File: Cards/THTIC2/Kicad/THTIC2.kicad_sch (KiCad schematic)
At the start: 26 parts, among them J1 Conn_01x04_Pin, J2 Plasma 300V, U1 B0509S-1WR3, U2 ISO1540, U3 ADS1014IDGS, U4 AMS1117-5, U5 LMV321

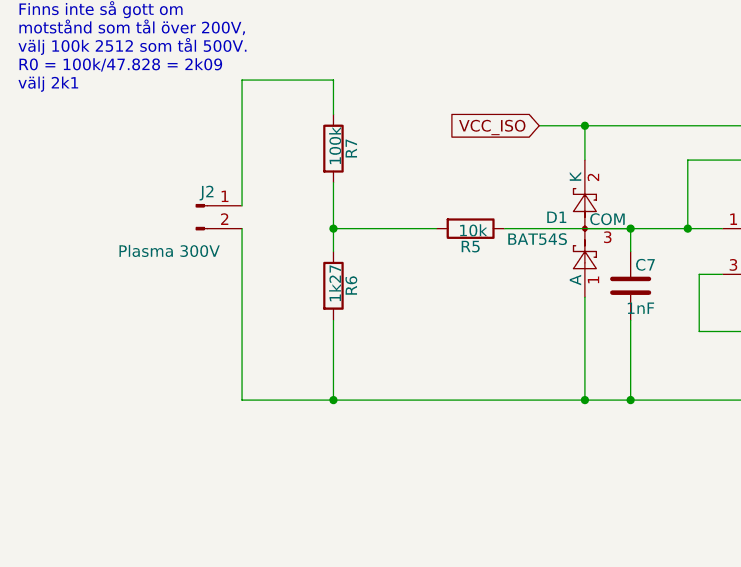
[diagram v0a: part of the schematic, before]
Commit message: Name change of E7000
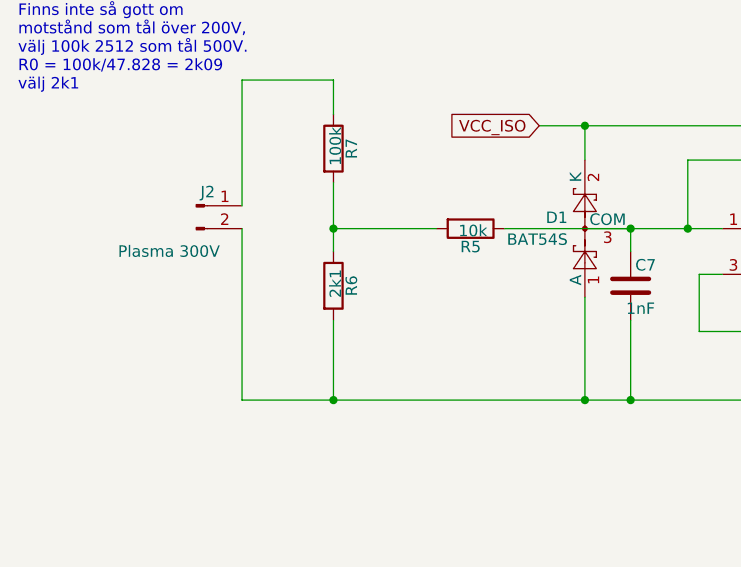
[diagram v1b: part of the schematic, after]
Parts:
- R6: value 1k27 -> 2k1
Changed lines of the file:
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@@
 			)
 		)
-		(property "Value" "1k27"
+		(property "Value" "2k1"
 			(at 52.324 82.296 90)
 			(effects

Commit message: Final version of THTIC2
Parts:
- added R8: 2k2, Resistor_SMD:R_0805_2012Metric, symbol Device:R
- R4: value nP -> 2k2
- renumbered H2 to H4
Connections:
- net 5V: now also R4.1, R8.1
- net at C7.1, D1.3 (COM), R5.1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: no longer R4.2
- net at R3.2, U5.3 (-), U5.4: no longer R4.1
- net at J1.2 (Pin_2), U2.2 (SDA1): now also R4.2
- net at J1.3 (Pin_3), U2.3 (SCL1): now also R8.2
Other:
- note added: "Optional pullups"
- moved on the sheet: J1

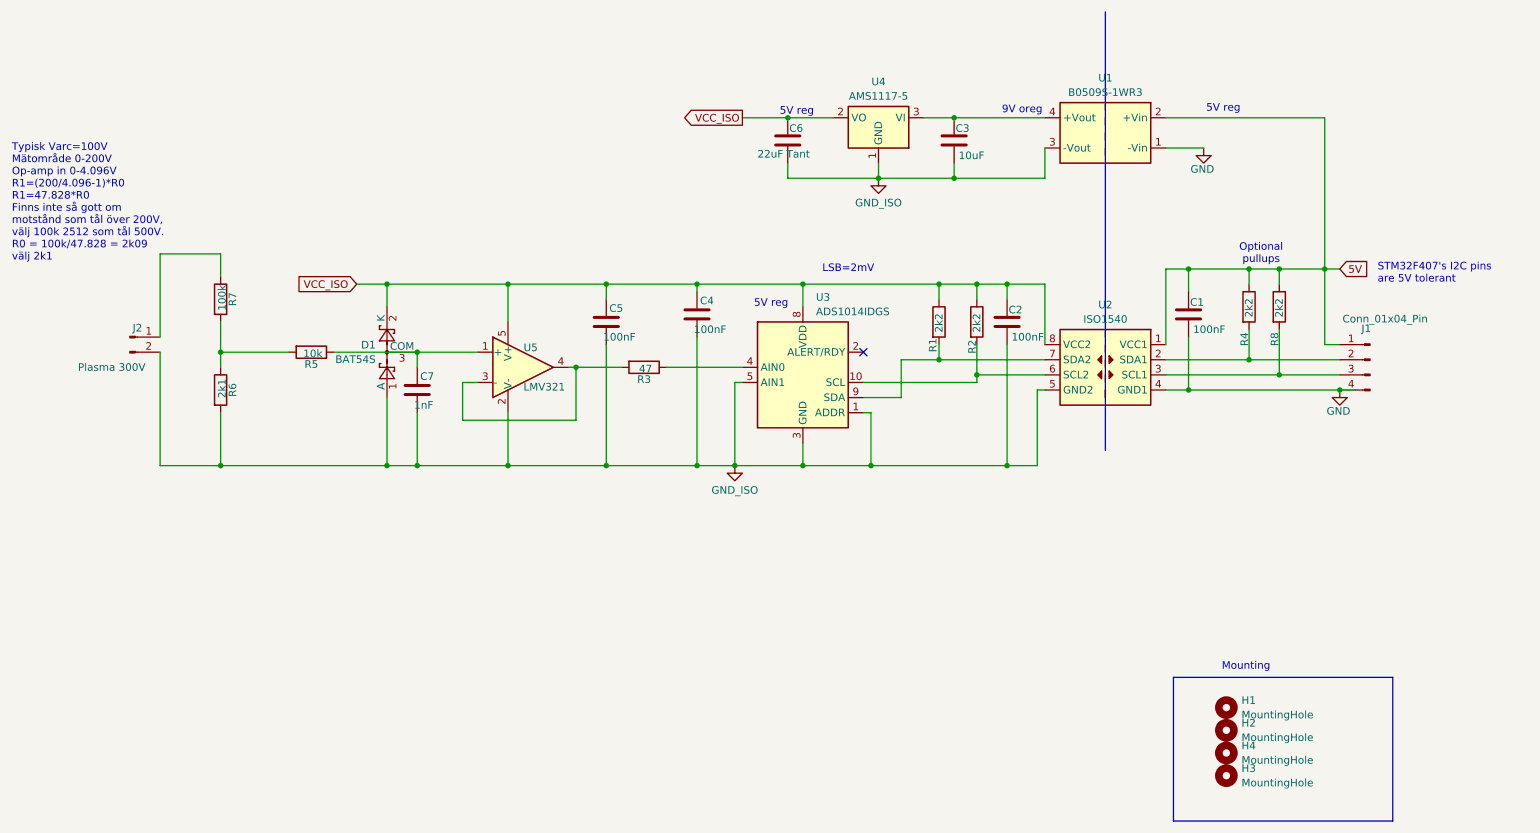
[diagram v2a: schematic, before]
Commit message: Now measuring 0 - -200 Volts.
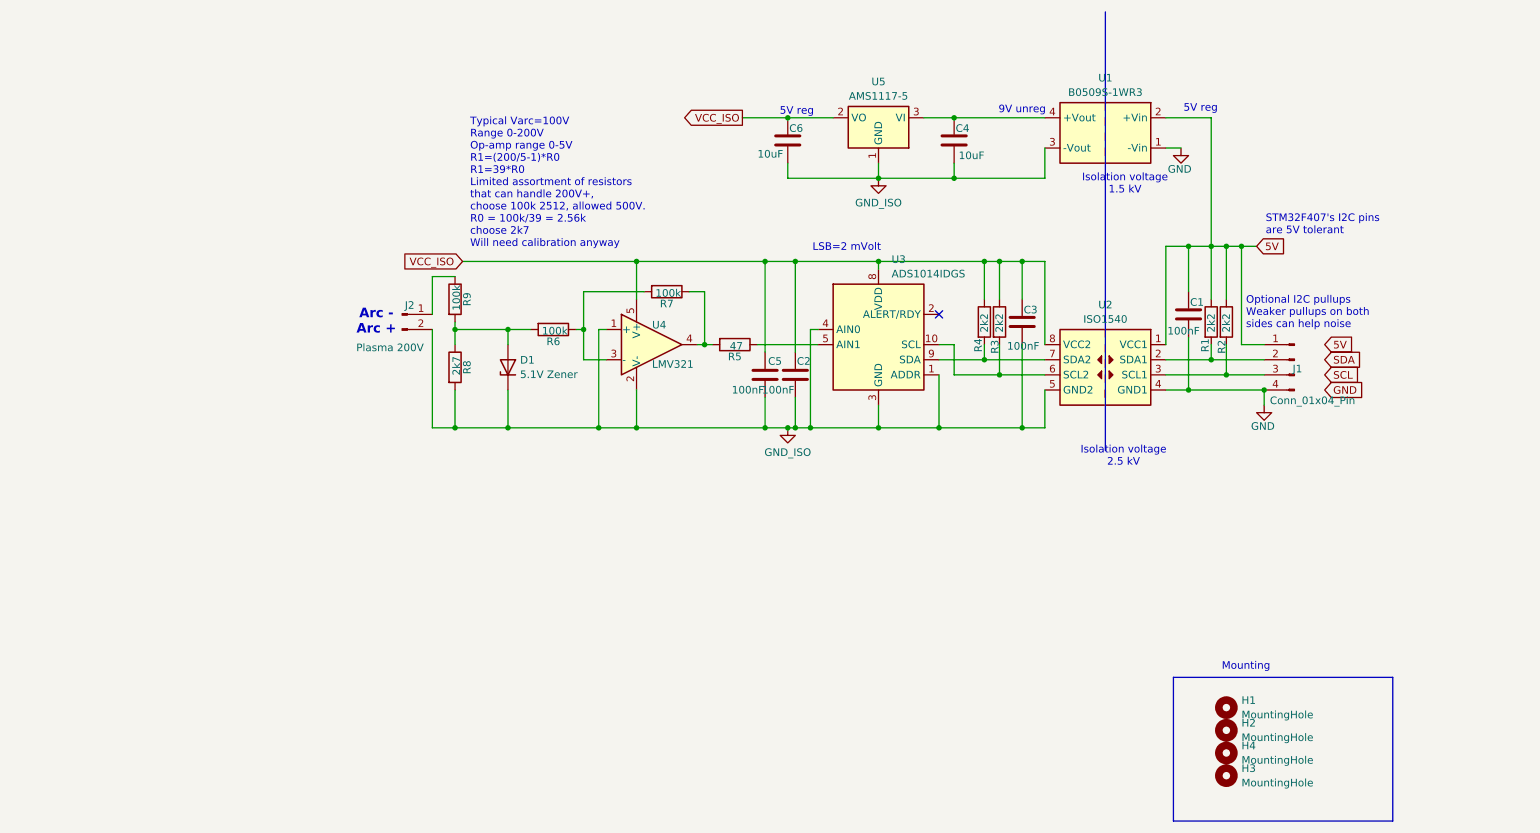
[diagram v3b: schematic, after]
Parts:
- removed C5: 100nF, Capacitor_SMD:C_0805_2012Metric, symbol Device:C
- removed C7: 1nF, Capacitor_SMD:C_0805_2012Metric, symbol Device:C
- removed D1: BAT54S, Package_TO_SOT_SMD:SOT-23, symbol Diode:BAT54S
- removed R4, R8: 2k2, Resistor_SMD:R_0805_2012Metric, symbol Device:R
- removed R5: 10k, Resistor_SMD:R_0805_2012Metric, symbol Device:R
- added C2: 100nF, Capacitor_SMD:C_0805_2012Metric, symbol Device:C
- added D1: 5.1V Zener, Diode_SMD:D_SOD-323_HandSoldering, symbol Device:D_Zener
- added R1, R2: 2k2, Resistor_SMD:R_0805_2012Metric, symbol Device:R
- added R6, R7: 100k, Resistor_SMD:R_0805_2012Metric, symbol Device:R
- C6: value 22uF Tant -> 10uF
- J2: value Plasma 300V -> Plasma 200V
- R8: renamed from R6; value 2k1 -> 2k7
- renumbered C2 to C3, C3 to C4, C4 to C5, R2 to R3, R1 to R4, R3 to R5, R7 to R9, U5 to U4, U4 to U5
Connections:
- net 5V: now also R1.1, R2.1
- net GND_ISO: now also U3.4 (AIN0), U4.1 (+), C2.2, D1.1 (K); no longer U3.5 (AIN1)
- net VCC_ISO: now also C2.1
- net at R8.1, R9.2: now also D1.2 (A), R6.2
- net at R5.2, U4.4: now also R7.1; no longer U4.3 (-)
- net at J1.2 (Pin_2), U2.2 (SDA1): now also R1.2
- net at J1.3 (Pin_3), U2.3 (SCL1): now also R2.2
- net at R5.1: now also U3.5 (AIN1); no longer U3.4 (AIN0)
- new net: R6.1, R7.2, U4.3 (-)
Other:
- note added: "9V unreg"
- note added: "Arc - Arc +"
- note added: "Isolation voltage 1.5 kV"
- note added: "Isolation voltage 2.5 kV"
- note added: "LSB=2 mVolt"
- note added: "Optional I2C pullups Weaker pullups on both sides can help noise"
- note added: "Typical Varc=100V Range 0-200V Op-amp range 0-5V R1=(200/5-1)*R0 R1=39*R0 Limited assortment of resistors that can handle 200V+, choose 100k 2512, allowed 500V. R0 = 100k/39 = 2.56k choose 2k7 Will need calibration anyway"
- note removed: "9V oreg"
- note removed: "LSB=2mV"
- note removed: "Optional pullups"
- note removed: "Typisk Varc=100V Mätområde 0-200V Op-amp in 0-4.096V R1=(200/4.096-1)*R0 R1=47.828*R0 Finns inte så gott om motstånd som tål över 200V, välj 100k 2512 som tål 500V. R0 = 100k/47.828 = 2k09 välj 2k1"
- moved on the sheet: C3, C5, J1, J2, R3, R4, R5, R8, R9, U4

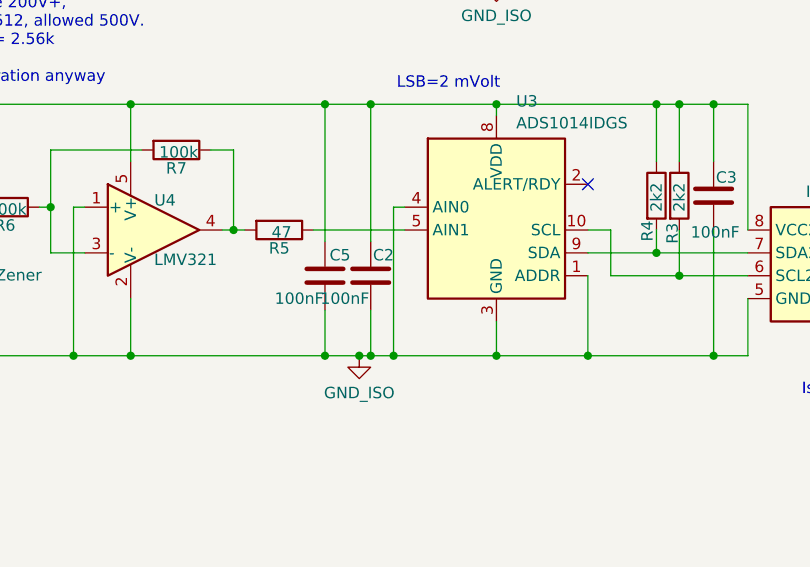
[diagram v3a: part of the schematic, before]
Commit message: Shifted pin 0 and pin 1 for positive voltage value.
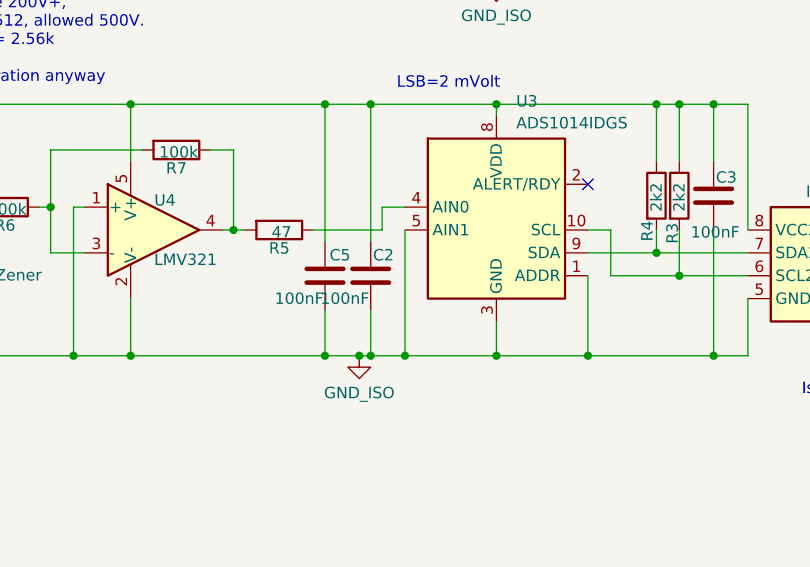
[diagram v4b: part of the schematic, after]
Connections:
- net GND_ISO: now also U3.5 (AIN1); no longer U3.4 (AIN0)
- net at R5.1: now also U3.4 (AIN0); no longer U3.5 (AIN1)
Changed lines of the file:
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@@
-	)
-	(junction
-		(at 151.13 88.9)
-		(diameter 0)
-		(color 0 0 0 0)
 	)
 	(junction
@@
 	(junction
 		(at 121.92 60.96)
+		(diameter 0)
+		(color 0 0 0 0)
+	)
+	(junction
+		(at 152.4 88.9)
 		(diameter 0)
 		(color 0 0 0 0)
@@
 	(wire
 		(pts
-			(xy 142.24 74.93) (xy 152.4 74.93)
-		)
-		(stroke
-			(width 0)
-			(type default)
-		)
-	)
-	(wire
-		(pts
 			(xy 121.92 60.96) (xy 121.92 67.31)
 		)
@@
 	(wire
 		(pts
-			(xy 151.13 72.39) (xy 152.4 72.39)
-		)
-		(stroke
-			(width 0)
-			(type default)
-		)
-	)
-	(wire
-		(pts
 			(xy 162.56 60.96) (xy 162.56 62.23)
 		)
@@
 	(wire
 		(pts
-			(xy 148.59 88.9) (xy 151.13 88.9)
-		)
-		(stroke
-			(width 0)
-			(type default)
-		)
-	)
-	(wire
-		(pts
 			(xy 175.26 80.01) (xy 175.26 74.93)
 		)
@@
 	(wire
 		(pts
-			(xy 151.13 88.9) (xy 162.56 88.9)
+			(xy 148.59 88.9) (xy 152.4 88.9)
 		)
 		(stroke
@@
 	(wire
 		(pts
+			(xy 149.86 72.39) (xy 152.4 72.39)
+		)
+		(stroke
+			(width 0)
+			(type default)
+		)
+	)
+	(wire
+		(pts
 			(xy 143.51 60.96) (xy 143.51 76.2)
 		)
@@
 	(wire
 		(pts
+			(xy 142.24 74.93) (xy 149.86 74.93)
+		)
+		(stroke
+			(width 0)
+			(type default)
+		)
+	)
+	(wire
+		(pts
 			(xy 113.03 66.04) (xy 113.03 72.39)
 		)
@@
 	(wire
 		(pts
+			(xy 149.86 74.93) (xy 149.86 72.39)
+		)
+		(stroke
+			(width 0)
+			(type default)
+		)
+	)
+	(wire
+		(pts
 			(xy 87.63 72.39) (xy 87.63 88.9)
 		)
@@
 	(wire
 		(pts
+			(xy 152.4 74.93) (xy 152.4 88.9)
+		)
+		(stroke
+			(width 0)
+			(type default)
+		)
+	)
+	(wire
+		(pts
 			(xy 143.51 88.9) (xy 147.32 88.9)
 		)
@@
 	(wire
 		(pts
-			(xy 151.13 72.39) (xy 151.13 88.9)
-		)
-		(stroke
-			(width 0)
-			(type default)
-		)
-	)
-	(wire
-		(pts
 			(xy 87.63 88.9) (xy 91.44 88.9)
 		)
 		(stroke
+			(width 0)
+			(type default)
+		)
+	)
+	(wire
+		(pts
+			(xy 152.4 88.9) (xy 162.56 88.9)
+		)
+		(stroke

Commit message: Upload changes
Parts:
- R8: value 2k7 -> 2k
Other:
- note added: "Typical Varc=100V Range 0-200V Op-amp range 0-4V R1=(200/4-1)*R0 R1=49*R0 Limited assortment of resistors that can handle 200V+, choose 100k 2512, allowed 500V. R0 = 100k/49 = 2.04k choose 2k Will need calibration anyway"
- note removed: "Typical Varc=100V Range 0-200V Op-amp range 0-5V R1=(200/5-1)*R0 R1=39*R0 Limited assortment of resistors that can handle 200V+, choose 100k 2512, allowed 500V. R0 = 100k/39 = 2.56k choose 2k7 Will need calibration anyway"
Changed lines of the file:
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@@
 		)
 	)
-	(text "Typical Varc=100V\nRange 0-200V\nOp-amp range 0-5V\nR1=(200/5-1)*R0\nR1=39*R0\nLimited assortment of resistors \nthat can handle 200V+,\nchoose 100k 2512, allowed 500V.\nR0 = 100k/39 = 2.56k\nchoose 2k7\nWill need calibration anyway"
+	(text "Typical Varc=100V\nRange 0-200V\nOp-amp range 0-4V\nR1=(200/4-1)*R0\nR1=49*R0\nLimited assortment of resistors \nthat can handle 200V+,\nchoose 100k 2512, allowed 500V.\nR0 = 100k/49 = 2.04k\nchoose 2k\nWill need calibration anyway"
 		(exclude_from_sim no)
 		(at 93.98 36.83 0)
@@
 			)
 		)
-		(property "Value" "2k7"
+		(property "Value" "2k"
 			(at 91.694 78.486 90)
 			(effects
